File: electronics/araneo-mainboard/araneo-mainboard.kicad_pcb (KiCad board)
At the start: 2 copper layers, 71.5 x 68.5 mm, 59 parts, among them J1 GPIO, J2 OLED, SW1 SW, U1 IMU, U2 L78M05CDT, U3 BD9C601EFJ, U4 POWER, U5 PAM8403D

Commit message: electronics: board pcb
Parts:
- removed LED1: Diode1, Connector_PinHeader_2.54mm:PinHeader_1x02_P2.54mm_Vertical
- removed LED2: Diode2, Connector_PinHeader_2.54mm:PinHeader_1x02_P2.54mm_Vertical
- removed LED3: Diode3, Connector_PinHeader_2.54mm:PinHeader_1x02_P2.54mm_Vertical
- removed R4, R5, R6: 4.7k, Resistor_SMD:R_0603_1608Metric_Pad0.98x0.95mm_HandSolder
- added D3: DEBUG_LED, PCM_SparkFun-LED:LED_0603_1608Metric, F.Cu at (118.5, 100.0)
- added H5: MountingHole, MountingHole:MountingHole_2.1mm, F.Cu at (2.38, 2.38)
- added R10: 4.7k, Resistor_SMD:R_0603_1608Metric_Pad0.98x0.95mm_HandSolder, F.Cu at (139.5, 71.5)
- added R11: 10k, Resistor_SMD:R_0603_1608Metric_Pad0.98x0.95mm_HandSolder, F.Cu at (137.5, 69.5)
- added R13: 1k, Resistor_SMD:R_0603_1608Metric_Pad0.98x0.95mm_HandSolder, F.Cu at (115.0, 100.0)
- D2: value POWER_LED -> BUCK_LED
- J1: footprint Connector_PinHeader_2.54mm:PinHeader_1x08_P2.54mm_Vertical -> Connector_PinHeader_2.54mm:PinHeader_1x09_P2.54mm_Vertical
- J2: footprint Connector_PinHeader_2.54mm:PinHeader_1x04_P2.54mm_Vertical -> PCM_SparkFun-Connector:ScrewTerminal_1x04_P3.5mm_Locking
- SW1: footprint Connector_PinHeader_2.54mm:PinHeader_1x02_P2.54mm_Vertical -> PCM_SparkFun-Connector:ScrewTerminal_1x02_P5.0mm
- moved R7 49.0 mm to (114.0, 57.5), turned to 90 degrees
- moved D2 45.1 mm to (116.0, 57.5), turned to 90 degrees
- moved U4 21.1 mm to (113.0, 40.0), turned to 0 degrees
- moved ? 18.1 mm to (138.0, 44.5)
- moved F1 13.8 mm to (102.3, 41.0), turned to -90 degrees
- moved SW1 13.5 mm to (112.5, 47.0), turned to -90 degrees
- moved J2 12.9 mm to (152.0, 100.3), turned to 90 degrees
- moved C11 4.53 mm to (154.5, 58.5)
- moved U2 4.47 mm to (147.6, 41.0)
- moved C14 4.17 mm to (156.0, 75.9), turned to 90 degrees
- moved FB1 4.03 mm to (154.5, 61.0)
- moved C17 4.00 mm to (150.5, 48.6)
- moved U1 3.94 mm to (146.0, 76.6)
- moved D1 3.54 mm to (158.5, 55.6)
- moved C18 3.50 mm to (150.0, 63.5)
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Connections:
- A1 pad 19: /D2 -> /GPIO14
- A1 pad 20: /D3 -> /GPIO15
- A1 pad 34: /GPIO28 -> /MEASURE
- F1 pad 1: Net-(SW1-B) -> +7.4V
- F1 pad 2: +7.4V -> Net-(SW1-A)
- J1 pad 5: /GPIO16 -> /GPIO14
- J1 pad 6: /GPIO17 -> /GPIO15
- J1 pad 7: /GPIO22 -> /GPIO16
- J1 pad 8: /GPIO28 -> /GPIO17
- J2 pad 1: /+3V3 -> /SDA_OLED
- J2 pad 2: GND -> /SCL_OLED
- J2 pad 3: /SCL_OLED -> GND
- J2 pad 4: /SDA_OLED -> /+3V3
- SW1 pad 1: /+7.4V_F -> Net-(SW1-A)
- SW1 pad 2: Net-(SW1-B) -> /+7.4V_F
- U4 pad 1: /+7.4V_F -> +7.4V
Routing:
- net /EN: track 0.00 -> 46.2 mm, vias 0 -> 3
- net /GPIO28: track 37.5 -> 0.00 mm
- net /GPIO15: track 0.00 -> 30.0 mm
- net /GPIO14: track 0.00 -> 27.2 mm, vias 0 -> 1
- net /D1: track 33.0 -> 8.49 mm
- net /+7.4V_F: track 60.1 -> 80.5 mm
- net /D3: track 16.9 -> 0.00 mm
- net /+3V3: track 33.7 -> 49.7 mm, vias 1 -> 0
- net /D2: track 11.1 -> 0.00 mm
- net Net-(U5-LOUT-): track 0.00 -> 6.11 mm
- net /SDA_OLED: track 9.85 -> 15.6 mm
- net /MEASURE: track 0.00 -> 5.54 mm, vias 0 -> 1
- net /SDA_IMU: track 7.08 -> 11.0 mm
- net /SCL_IMU: track 7.08 -> 11.0 mm
- net Net-(LED3-Pin_2): track 3.79 -> 0.00 mm
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- added copper zone on F.Cu, net +7.4V
- added copper zone on B.Cu, net GND
- added copper zone on F.Cu, net GND
- added copper zone on F.Cu, net Net-(SW1-A)
- removed copper zone on F.Cu, net Net-(SW1-B)
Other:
- board text added: "+"
- board text added: "3V3 GND SCL SDA"
- board text added: "DEBUG"
- board text added: "POWER"

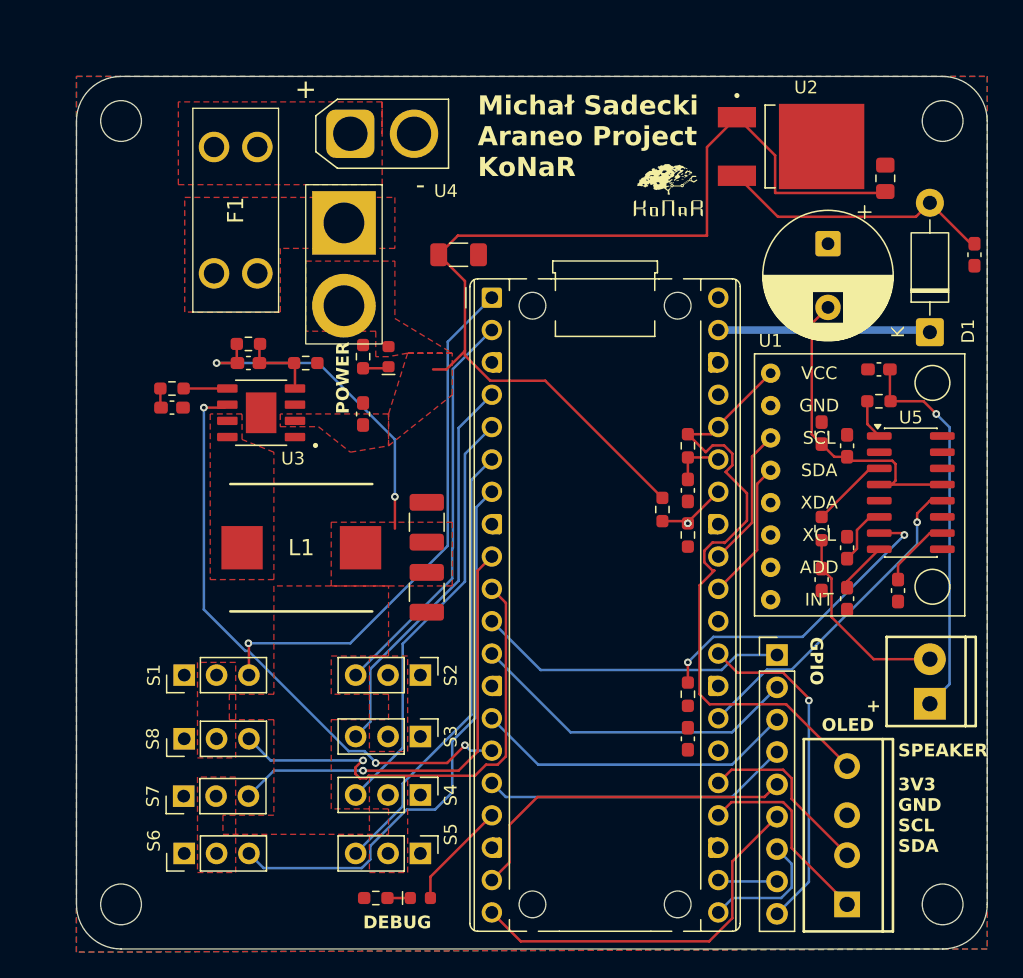
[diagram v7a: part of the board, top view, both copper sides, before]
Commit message: electronics: add button
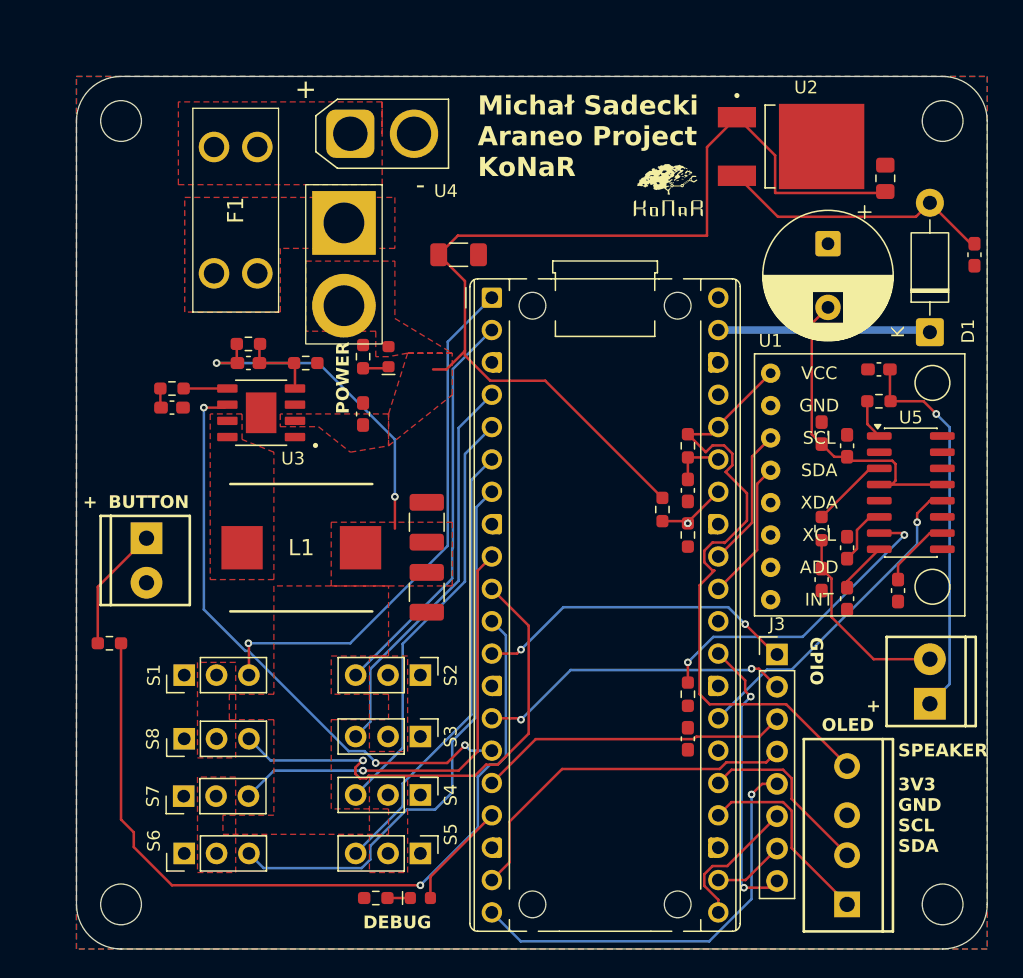
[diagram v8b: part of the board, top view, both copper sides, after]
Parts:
- removed J1: GPIO, Connector_PinHeader_2.54mm:PinHeader_1x09_P2.54mm_Vertical
- added J3: GPIO, Connector_PinHeader_2.54mm:PinHeader_1x08_P2.54mm_Vertical, F.Cu at (146.5, 80.9)
- added R14: 10k, Resistor_SMD:R_0603_1608Metric_Pad0.98x0.95mm_HandSolder, F.Cu at (94.1, 80.0)
- added SW2: SW, PCM_SparkFun-Connector:ScrewTerminal_1x02_P3.5mm_Blue, F.Cu at (97.0, 71.8)
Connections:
- A1 pad 11: /GPIO8 -> /BUTTON
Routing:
- net /BUTTON: track 0.00 -> 64.5 mm, vias 0 -> 1
- net /GPIO8: track 24.5 -> 0.00 mm, vias 1 -> 0
- net Net-(SW2-A): track 0.00 -> 9.83 mm
- net /GPIO22: track 26.5 -> 22.6 mm, vias 1 -> 2
- net /GPIO15: track 30.0 -> 33.3 mm, vias 0 -> 1
- net /PWM8: track 37.3 -> 38.7 mm
- net /GPIO14: track 27.2 -> 28.4 mm, vias 1 -> 0
- net /GPIO16: track 10.1 -> 11.0 mm
- net /GPIO17: track 4.66 -> 5.63 mm
- net /GPIO9: track 26.4 -> 25.4 mm, vias 0 -> 2
- net /GPIO10: track 25.4 -> 24.7 mm, vias 0 -> 2
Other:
- board text added: "22.07.2026 Projekt inżynierski prowadzony przez Mateusza Cholewińskiego"
- board text added: "BUTTON"
- board text removed: "15.07.2026 Projekt inżynierski prowadzony przez Mateusza Cholewińskiego"
